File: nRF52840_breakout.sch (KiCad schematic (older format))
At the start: 39 parts, among them J7 Conn_Coaxial, U1 nRF52840, U5 MM8130-2600RA2, Y1 SiT1533, Y2 32MHz-XRCGB32M000F1H00R0

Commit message: layout / added part details etc
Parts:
- removed AE1: Antenna, RF_Antenna:Texas_SWRA117D_2.4GHz_Right, symbol Device:Antenna
- added AE1: TI_SWRA117D, RF_Antenna:Texas_SWRA117D_2.4GHz_Right, symbol Device:Antenna_Shield
- C25, L1, R4: value NC -> N.C.
- J7: value Conn_Coaxial -> U.FL_A-1JB
- R13, R14, R15: value 1.5k -> 180R
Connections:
- net GND: now also AE1.2 (Shield)
- net at R11.1: now also AE1.1 (A)
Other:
- note added: "RGB-LED"
- moved on the sheet: D3, R13, R14, R15
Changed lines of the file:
@@
 P 4000 4450
 F 0 "L1" V 3850 4450 50  0000 C CNN
-F 1 "NC" V 3950 4450 50  0000 C CNN
+F 1 "N.C." V 3950 4450 50  0000 C CNN
 F 2 "Inductor_SMD:L_0402_1005Metric" H 4000 4450 50  0001 C CNN
 F 3 "~" H 4000 4450 50  0001 C CNN
@@
 	4950 5500 4600 5500
 Wire Wire Line
-	4950 5150 4950 5500
+	4950 5150 4950 5250
 Connection ~ 4600 5500
 Wire Wire Line
@@
 S 950  1650 750  200
 U 5C9D648D
-F0 "Todo" 50
-F1 "nRF52840_breakout_todo.sch" 50
+F0 "Sensor" 50
+F1 "nRF52840_breakout_sensor.sch" 50
 $EndSheet
 Wire Wire Line
-	3250 4350 4350 4350
+	3250 4350 3550 4350
 Wire Wire Line
 	3250 4350 3250 4800
@@
 P 2200 4950
 F 0 "C25" H 2292 4996 50  0000 L CNN
-F 1 "NC" H 2292 4905 50  0000 L CNN
+F 1 "N.C." H 2292 4905 50  0000 L CNN
 F 2 "Capacitor_SMD:C_0402_1005Metric" H 2200 4950 50  0001 C CNN
 F 3 "~" H 2200 4950 50  0001 C CNN
@@
 P 2400 4800
 F 0 "R4" V 2246 4800 50  0000 C CNN
-F 1 "NC" V 2326 4800 50  0000 C CNN
+F 1 "N.C." V 2326 4800 50  0000 C CNN
 F 2 "Resistor_SMD:R_0402_1005Metric" H 2400 4800 50  0001 C CNN
 F 3 "~" H 2400 4800 50  0001 C CNN
@@
 P 10300 2350
 F 0 "J7" H 10399 2326 50  0000 L CNN
-F 1 "Conn_Coaxial" H 10399 2235 50  0000 L CNN
+F 1 "U.FL_A-1JB" H 10399 2235 50  0000 L CNN
 F 2 "custom_footprints:CON_AMP_A-1JB" H 10300 2350 50  0001 C CNN
 F 3 " ~" H 10300 2350 50  0001 C CNN
@@
 	9200 3250 9300 3250
 Connection ~ 9300 3250
-Wire Wire Line
-	9800 1700 9800 1750
 $Comp
 L CONN_SWF:MM8130-2600RA2 U5
@@
 Wire Wire Line
 	8850 3450 8850 3500
-$Comp
-L Device:Antenna AE1
-U 1 1 5CCC95CB
-P 9800 1500
-F 0 "AE1" H 9880 1491 50  0000 L CNN
-F 1 "Antenna" H 9880 1400 50  0000 L CNN
-F 2 "RF_Antenna:Texas_SWRA117D_2.4GHz_Right" H 9800 1500 50  0001 C CNN
-F 3 "~" H 9800 1500 50  0001 C CNN
-	1    9800 1500
-	1    0    0    -1
-$EndComp
 Connection ~ 9900 3250
 Wire Wire Line
@@
 Wire Wire Line
 	2850 2150 2800 2150
-Text GLabel 10150 5700 2    50   Input ~ 0
+Text GLabel 10650 6100 2    50   Input ~ 0
 VDD_nRF
 Wire Wire Line
-	9550 5500 9500 5500
-Wire Wire Line
-	9550 5700 9500 5700
-Wire Wire Line
-	9550 5900 9500 5900
-Text GLabel 9300 5900 0    50   Input ~ 0
+	10050 5900 10000 5900
+Wire Wire Line
+	10050 6100 10000 6100
+Wire Wire Line
+	10050 6300 10000 6300
+Text GLabel 9800 6300 0    50   Input ~ 0
 P1.08
-Text GLabel 9300 5700 0    50   Input ~ 0
+Text GLabel 9800 6100 0    50   Input ~ 0
 P1.09
-Text GLabel 9300 5500 0    50   Input ~ 0
+Text GLabel 9800 5900 0    50   Input ~ 0
 P1.10
 $Comp
 L Device:R_Small R13
 U 1 1 5CDA0CC5
-P 9400 5500
-F 0 "R13" V 9399 5495 50  0000 C CNN
-F 1 "1.5k" V 9462 5501 50  0000 C CNN
-F 2 "Resistor_SMD:R_0402_1005Metric" H 9400 5500 50  0001 C CNN
-F 3 "~" H 9400 5500 50  0001 C CNN
-	1    9400 5500
+P 9900 5900
+F 0 "R13" V 9899 5895 50  0000 C CNN
+F 1 "180R" V 9962 5901 50  0000 C CNN
+F 2 "Resistor_SMD:R_0402_1005Metric" H 9900 5900 50  0001 C CNN
+F 3 "~" H 9900 5900 50  0001 C CNN
+	1    9900 5900
 	0    1    1    0
 $EndComp
@@
 L Device:R_Small R14
 U 1 1 5CDA0D5D
-P 9400 5700
-F 0 "R14" V 9401 5697 50  0000 C CNN
-F 1 "1.5k" V 9464 5698 50  0000 C CNN
-F 2 "Resistor_SMD:R_0402_1005Metric" H 9400 5700 50  0001 C CNN
-F 3 "~" H 9400 5700 50  0001 C CNN
-	1    9400 5700
+P 9900 6100
+F 0 "R14" V 9901 6097 50  0000 C CNN
+F 1 "180R" V 9964 6098 50  0000 C CNN
+F 2 "Resistor_SMD:R_0402_1005Metric" H 9900 6100 50  0001 C CNN
+F 3 "~" H 9900 6100 50  0001 C CNN
+	1    9900 6100
 	0    1    1    0
 $EndComp
@@
 L Device:R_Small R15
 U 1 1 5CDA0DBD
-P 9400 5900
-F 0 "R15" V 9400 5892 50  0000 C CNN
-F 1 "1.5k" V 9472 5897 50  0000 C CNN
-F 2 "Resistor_SMD:R_0402_1005Metric" H 9400 5900 50  0001 C CNN
-F 3 "~" H 9400 5900 50  0001 C CNN
-	1    9400 5900
+P 9900 6300
+F 0 "R15" V 9900 6292 50  0000 C CNN
+F 1 "180R" V 9972 6297 50  0000 C CNN
+F 2 "Resistor_SMD:R_0402_1005Metric" H 9900 6300 50  0001 C CNN
+F 3 "~" H 9900 6300 50  0001 C CNN
+	1    9900 6300
 	0    1    1    0
 $EndComp
@@
 L LTST-C19HE1WT:LTST-C19HE1WT D3
 U 1 1 5CDACEAD
-P 9750 5700
-F 0 "D3" H 9850 6181 50  0000 C CNN
-F 1 "LTST-C19HE1WT" H 9850 6090 50  0000 C CNN
-F 2 "custom_footprints:LTST-C19HE1WT" H 9750 5700 50  0001 L BNN
-F 3 "Unavailable" H 9750 5700 50  0001 L BNN
-F 4 "0606 Lite-On" H 9750 5700 50  0001 L BNN "Field4"
-F 5 "None" H 9750 5700 50  0001 L BNN "Field5"
-F 6 "LTST-C19HE1WT" H 9750 5700 50  0001 L BNN "Field6"
-F 7 "R/G/B 0606 Flat Top Rectangle 130° 112.5/281/104 mcd Diffused Chip LED" H 9750 5700 50  0001 L BNN "Field7"
-F 8 "Lite-On Inc." H 9750 5700 50  0001 L BNN "Field8"
-	1    9750 5700
-	1    0    0    -1
-$EndComp
+P 10250 6100
+F 0 "D3" H 10350 6581 50  0000 C CNN
+F 1 "LTST-C19HE1WT" H 10350 6490 50  0000 C CNN
+F 2 "custom_footprints:LTST-C19HE1WT" H 10250 6100 50  0001 L BNN
+F 3 "Unavailable" H 10250 6100 50  0001 L BNN
+F 4 "0606 Lite-On" H 10250 6100 50  0001 L BNN "Field4"
+F 5 "None" H 10250 6100 50  0001 L BNN "Field5"
+F 6 "LTST-C19HE1WT" H 10250 6100 50  0001 L BNN "Field6"
+F 7 "R/G/B 0606 Flat Top Rectangle 130° 112.5/281/104 mcd Diffused Chip LED" H 10250 6100 50  0001 L BNN "Field7"
+F 8 "Lite-On Inc." H 10250 6100 50  0001 L BNN "Field8"
+	1    10250 6100
+	1    0    0    -1
+$EndComp
+$Comp
+L Device:Antenna_Shield AE1
+U 1 1 5CCC4E43
+P 9800 1200
+F 0 "AE1" H 9940 1241 50  0000 L CNN
+F 1 "TI_SWRA117D" H 9940 1150 50  0000 L CNN
+F 2 "RF_Antenna:Texas_SWRA117D_2.4GHz_Right" H 9800 1300 50  0001 C CNN
+F 3 "~" H 9800 1300 50  0001 C CNN
+	1    9800 1200
+	1    0    0    -1
+$EndComp
+$Comp
+L power:GND #PWR0110
+U 1 1 5CCC501D
+P 9900 1450
+F 0 "#PWR0110" H 9900 1200 50  0001 C CNN
+F 1 "GND" H 9905 1277 50  0000 C CNN
+F 2 "" H 9900 1450 50  0001 C CNN
+F 3 "" H 9900 1450 50  0001 C CNN
+	1    9900 1450
+	1    0    0    -1
+$EndComp
+Wire Wire Line
+	9800 1400 9800 1750
+Wire Wire Line
+	9900 1400 9900 1450
+$Comp
+L power:PWR_FLAG #FLG0101
+U 1 1 5CCDA706
+P 4950 5250
+F 0 "#FLG0101" H 4950 5325 50  0001 C CNN
+F 1 "PWR_FLAG" V 4950 5378 50  0000 L CNN
+F 2 "" H 4950 5250 50  0001 C CNN
+F 3 "~" H 4950 5250 50  0001 C CNN
+	1    4950 5250
+	0    -1   -1   0
+$EndComp
+Connection ~ 4950 5250
+Wire Wire Line
+	4950 5250 4950 5500
+$Comp
+L power:PWR_FLAG #FLG0102
+U 1 1 5CCDA9ED
+P 3550 4350
+F 0 "#FLG0102" H 3550 4425 50  0001 C CNN
+F 1 "PWR_FLAG" H 3550 4523 50  0000 C CNN
+F 2 "" H 3550 4350 50  0001 C CNN
+F 3 "~" H 3550 4350 50  0001 C CNN
+	1    3550 4350
+	-1   0    0    1
+$EndComp
+Connection ~ 3550 4350
+Wire Wire Line
+	3550 4350 4350 4350
+Text Notes 9500 5500 0    50   ~ 0
+RGB-LED
+Wire Notes Line
+	9300 6500 9300 5400
+Wire Notes Line
+	9300 5400 11100 5400
+Wire Notes Line
+	11100 5400 11100 6500
+Wire Notes Line
+	11100 6500 9300 6500
 $EndSCHEMATC

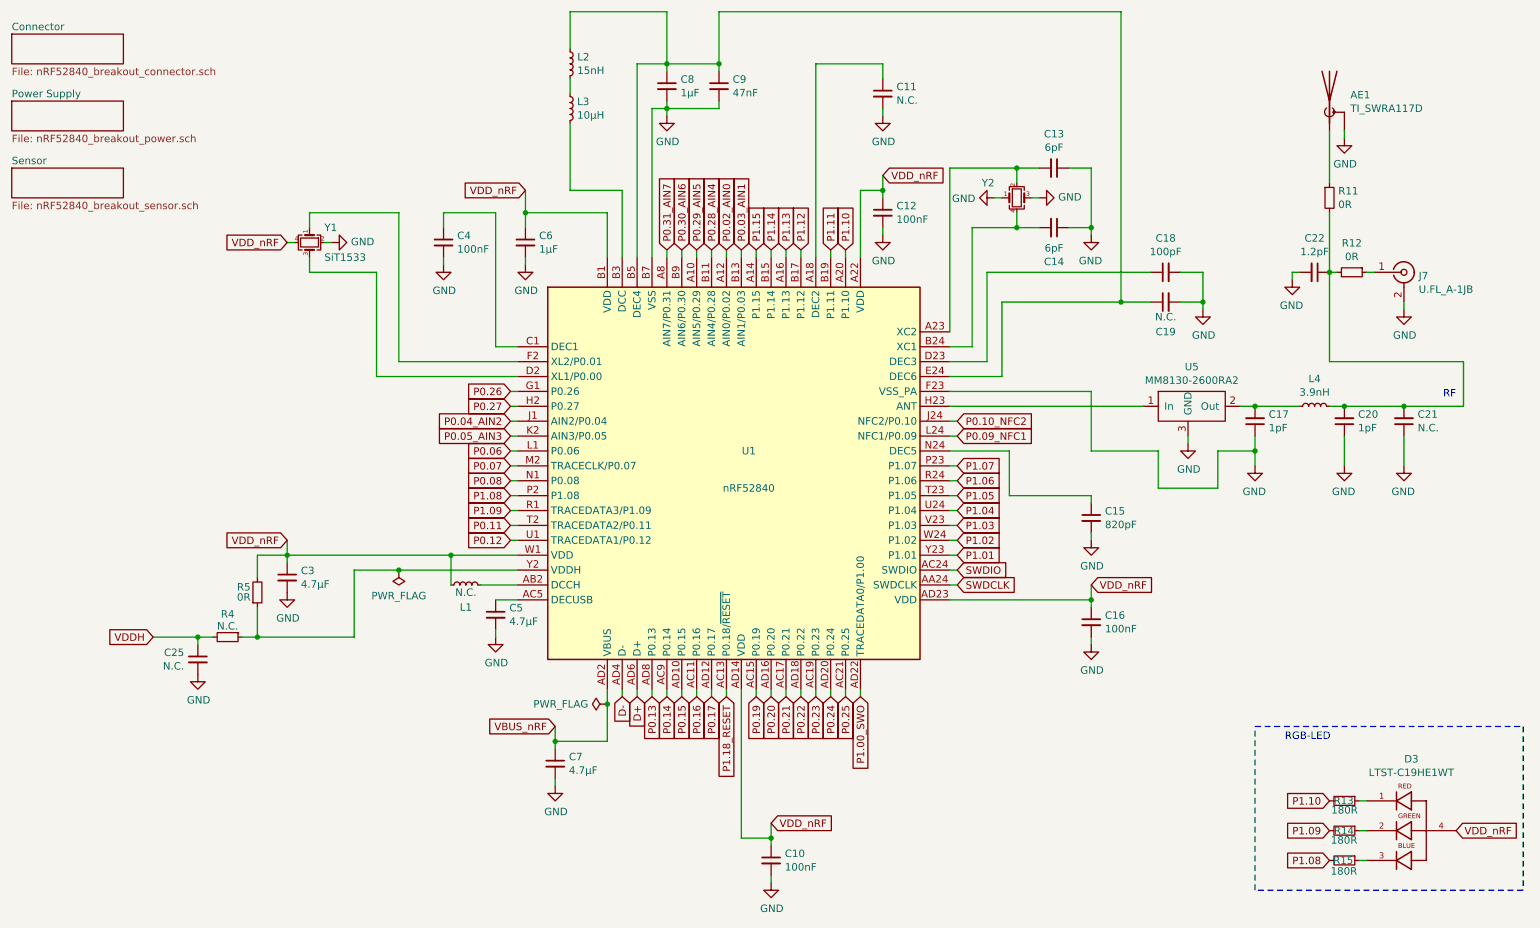
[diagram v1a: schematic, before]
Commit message: 2 layer som version
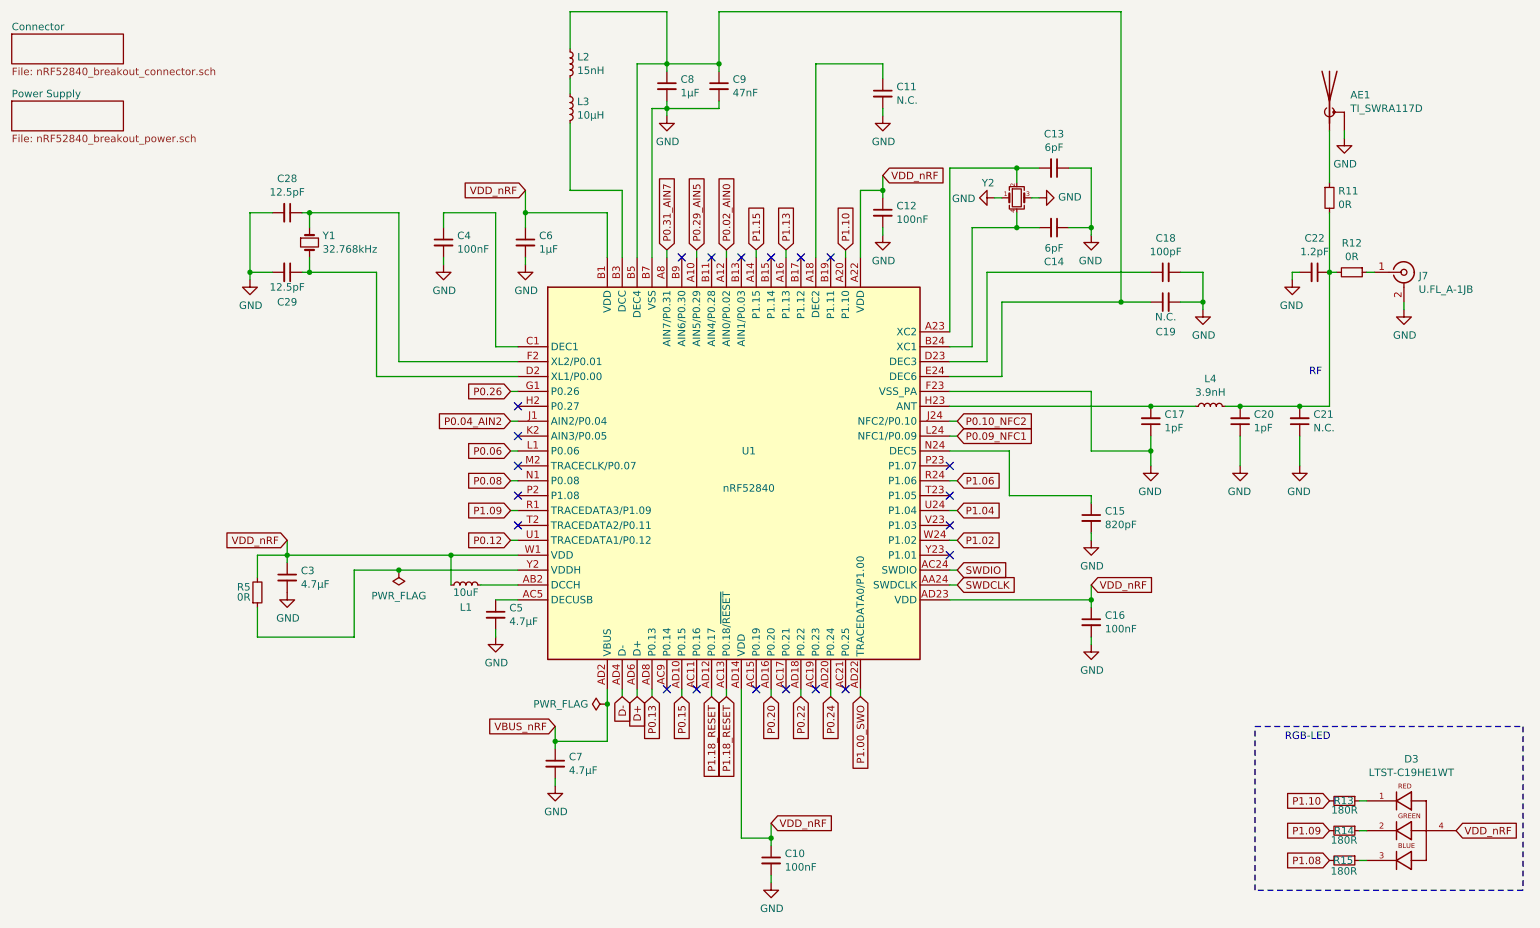
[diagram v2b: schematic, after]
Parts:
- removed C25: N.C., Capacitor_SMD:C_0402_1005Metric, symbol Device:C_Small
- removed R4: N.C., Resistor_SMD:R_0402_1005Metric, symbol Device:R_Small
- removed U5: MM8130-2600RA2, custom_footprints:MM8930_2620, symbol CONN_SWF:MM8130-2600RA2
- removed Y1: SiT1533, custom_footprints:Crystal_SMD_2012-4Pin_2.2mmx1.4mm, symbol Device:Crystal_GND24_Small
- added C28, C29: 12.5pF, Capacitor_SMD:C_0402_1005Metric, symbol Device:C_Small
- added Y1: 32.768kHz, Crystal:Crystal_SMD_3215-2Pin_3.2x1.5mm, symbol Device:Crystal_Small
- L1: value N.C. -> 10uF; DNP (none) -> 1
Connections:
- net P0.17 is gone; now on net P1.18_RESET: U1.AD12 (P0.17)
- net GND: now also C28.2, C29.2
- net P1.08: no longer U1.P2 (P1.08)
- net at C17.2, L4.2: now also U1.H23 (ANT)
- net at U1.D2 (XL1/P0.00): now also C29.1, Y1.2
- net at U1.F2 (XL2/P0.01): now also C28.1, Y1.1
- net P0.03_AIN1: no longer names the net of U1.B13 (AIN1/P0.03)
- net P0.05_AIN3: no longer names the net of U1.K2 (AIN3/P0.05)
- net P0.07: no longer names the net of U1.M2 (TRACECLK/P0.07)
- net P0.11: no longer names the net of U1.T2 (TRACEDATA2/P0.11)
- net P0.14: no longer names the net of U1.AC9 (P0.14)
- net P0.16: no longer names the net of U1.AC11 (P0.16)
- net P0.19: no longer names the net of U1.AC15 (P0.19)
- net P0.21: no longer names the net of U1.AC17 (P0.21)
- net P0.23: no longer names the net of U1.AC19 (P0.23)
- net P0.25: no longer names the net of U1.AC21 (P0.25)
- net P0.27: no longer names the net of U1.H2 (P0.27)
- net P0.28_AIN4: no longer names the net of U1.B11 (AIN4/P0.28)
- net P0.30_AIN6: no longer names the net of U1.B9 (AIN6/P0.30)
- net P1.01: no longer names the net of U1.Y23 (P1.01)
- net P1.03: no longer names the net of U1.V23 (P1.03)
- net P1.05: no longer names the net of U1.T23 (P1.05)
- net P1.07: no longer names the net of U1.P23 (P1.07)
- net P1.11: no longer names the net of U1.B19 (P1.11)
- net P1.12: no longer names the net of U1.B17 (P1.12)
- net P1.14: no longer names the net of U1.B15 (P1.14)
- no-connect marks 0 -> 21
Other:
- moved on the sheet: C17, C20, C21, L4

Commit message: modified bom / fixed silk,fab / added 3D models
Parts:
- removed D3: LTST-C19HE1WT, custom_footprints:LTST-C19HE1WT, symbol LTST-C19HE1WT:LTST-C19HE1WT
- removed R13, R14, R15: 180R, Resistor_SMD:R_0402_1005Metric, symbol Device:R_Small
- C10, C12, C16, C4: Description (none) -> CAP CER 0.1UF 10V X5R 0402; Digikey (none) -> 1276-1022-1-ND; LCSC (none) -> C159815; MFG P/N (none) -> CL05A104KP5NNNC; Manufacturer (none) -> Samsung Electro-Mechanics
- C11, C19, C21: DNP (none) -> 1
- C13, C14: value 6pF -> 8pF; Description (none) -> CAP CER 8PF 50V NPO 0402; Digikey (none) -> 311-3328-1-ND; LCSC (none) -> C130118; MFG P/N (none) -> CC0402CRNPO9BN8R0; Manufacturer (none) -> Yageo
- C15: Description (none) -> CAP CER 820PF 50V X7R 0402; Digikey (none) -> 1276-1589-1-ND; LCSC (none) -> C159810; MFG P/N (none) -> CL05B821KB5NNNC; Manufacturer (none) -> Samsung Electro-Mechanics
- C17, C20: Description (none) -> CAP CER 1PF 50V C0G/NPO 0402; Digikey (none) -> 311-2076-1-ND; LCSC (none) -> C277493; MFG P/N (none) -> CC0402CRNPO9BN1R0; Manufacturer (none) -> Yageo
- C18: Description (none) -> CAP CER 100PF 50V C0G/NPO 0402; Digikey (none) -> 311-1024-1-ND; LCSC (none) -> C106200; MFG P/N (none) -> CC0402JRNPO9BN101; Manufacturer (none) -> Yageo
- C22: Description (none) -> CAP CER 1.2PF 50V C0G/NPO 0402; Digikey (none) -> 311-1002-1-ND; LCSC (none) -> C277490; MFG P/N (none) -> CC0402CRNPO9BN1R2; Manufacturer (none) -> Yageo
- C28, C29: value 12.5pF -> 7pF; Description (none) -> CAP CER 7PF 50V C0G/NP0 0402; Digikey (none) -> 490-6254-1-ND; LCSC (none) -> C88936; MFG P/N (none) -> GRM1555C1H7R0BA01D; Manufacturer (none) -> Murata Electronics
- C3, C5, C7: value 4.7µF -> 4.7uF; Description (none) -> CAP CER 4.7UF 6.3V X5R 0402; Digikey (none) -> 587-2787-1-ND; LCSC (none) -> C87147; MFG P/N (none) -> JMK105BBJ475MV-F; Manufacturer (none) -> Taiyo Yuden
- C6, C8: value 1µF -> 1uF; Description (none) -> CAP CER 1UF 16V X5R 0402; Digikey (none) -> 1276-1067-1-ND; LCSC (none) -> C29266; MFG P/N (none) -> CL05A105KO5NNNC; Manufacturer (none) -> Samsung Electro-Mechanics
- C9: Description (none) -> CAP CER 0.047UF 50V X7R 0402; Digikey (none) -> 311-3815-1-ND; LCSC (none) -> C272875; MFG P/N (none) -> CC0402KRX7R9BB473; Manufacturer (none) -> Yageo
- J7: Description (none) -> CONN UMC JACK STR 50 OHM SMD; Digikey (none) -> ARF1579CT-ND; LCSC (none) -> C88373; MFG P/N (none) -> A-1JB; Manufacturer (none) -> Amphenol RF Division
- L1: value 10uF -> 10uH; footprint Inductor_SMD:L_0402_1005Metric -> Inductor_SMD:L_0603_1608Metric; Description (none) -> FIXED IND 10UH 50MA 900 MOHM SMD; Digikey (none) -> 490-4025-1-ND; LCSC (none) -> C86083; MFG P/N (none) -> LQM18FN100M00D; Manufacturer (none) -> Murata Electronics
- L2: Description (none) -> FIXED IND 15NH 460MA 160 MOHM; Digikey (none) -> 490-6771-1-ND; LCSC (none) -> C98055; MFG P/N (none) -> LQW15AN15NG00D; Manufacturer (none) -> Murata Electronics
- L3: value 10µH -> 10uH; footprint Inductor_SMD:L_0402_1005Metric -> Inductor_SMD:L_0603_1608Metric; Description (none) -> FIXED IND 10UH 50MA 900 MOHM SMD; Digikey (none) -> 490-4025-1-ND; LCSC (none) -> C86083; MFG P/N (none) -> LQM18FN100M00D; Manufacturer (none) -> Murata Electronics
- L4: Description (none) -> FIXED IND 3.9NH 700MA 190 MOHM; Digikey (none) -> 490-1079-1-ND; LCSC (none) -> C97987; MFG P/N (none) -> LQG15HN3N9S02D; Manufacturer (none) -> Murata Electronics
- R11, R12, R5: Description (none) -> RES SMD 0 OHM JUMPER 1/16W 0402; Digikey (none) -> 311-0.0JRCT-ND; LCSC (none) -> C60485; MFG P/N (none) -> RC0402JR-070RL; Manufacturer (none) -> Yageo
- U1: Description (none) -> IC RF TXRX+MCU 802.15.4 73VFQFN; Digikey (none) -> 1490-1071-1-ND; LCSC (none) -> C190794; MFG P/N (none) -> NRF52840-QIAA-R; Manufacturer (none) -> Nordic Semicon
- Y1: footprint Crystal:Crystal_SMD_3215-2Pin_3.2x1.5mm -> custom_footprints:Crystal_SMD_2012-2Pin_2.0x1.2mm; Description (none) -> CRYSTAL 32.7680KHZ 7PF SMD; Digikey (none) -> 728-1076-1-ND; LCSC (none) -> C97602; MFG P/N (none) -> SC20S-7PF20PPM; Manufacturer (none) -> Seiko Instruments
- Y2: value 32MHz-XRCGB32M000F1H00R0 -> 32MHz; footprint Crystal:Crystal_SMD_2016-4Pin_2.0x1.6mm -> custom_footprints:Crystal_SMD_2016-4Pin_2.0x1.6mm; Description (none) -> SMD Crystal Resonators 32MHz ±20ppm; LCSC (none) -> C108165; MFG P/N (none) -> X201632MKD4SI; Manufacturer (none) -> Yangxing Tech
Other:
- note removed: "RGB-LED"
